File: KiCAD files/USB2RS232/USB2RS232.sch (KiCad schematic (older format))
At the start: 8 parts

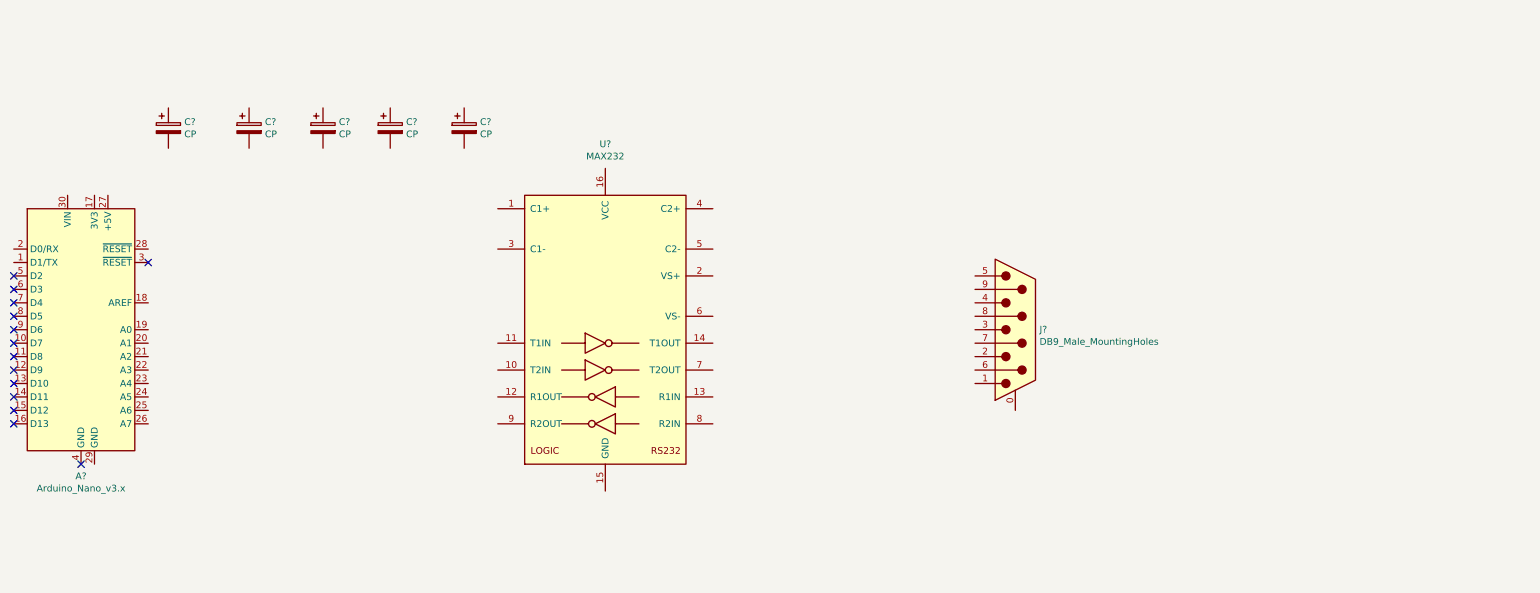
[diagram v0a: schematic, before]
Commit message: Update USB2RS232.sch
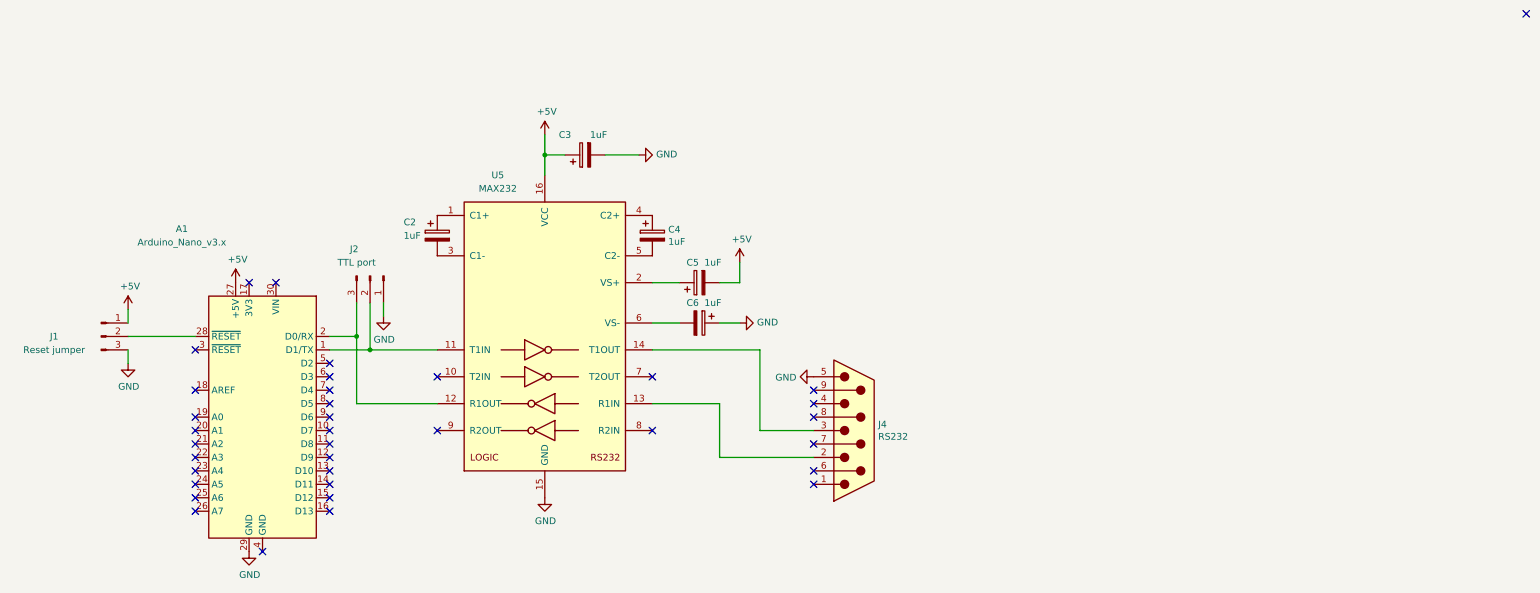
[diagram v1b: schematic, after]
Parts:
- removed A?: Arduino_Nano_v3.x, Module:Arduino_Nano, symbol MCU_Module:Arduino_Nano_v3.x
- removed C? (x5): CP, symbol Device:CP
- removed J?: DB9_Male_MountingHoles, symbol Connector:DB9_Male_MountingHoles
- removed U?: MAX232, symbol Interface_UART:MAX232
- added A1: Arduino_Nano_v3.x, Module:Arduino_Nano, symbol MCU_Module:Arduino_Nano_v3.x
- added C2, C3, C4, C5, C6: 1uF, Capacitor_THT:CP_Radial_D7.5mm_P2.50mm, symbol Device:CP
- added J1: Reset jumper, Connector_PinHeader_2.54mm:PinHeader_1x03_P2.54mm_Horizontal, symbol Connector:Conn_01x03_Male
- added J2: TTL port, Connector_PinHeader_2.54mm:PinHeader_1x03_P2.54mm_Horizontal, symbol Connector:Conn_01x03_Male
- added J4: RS232, Connector_Dsub:DSUB-9_Male_Horizontal_P2.77x2.54mm_EdgePinOffset9.40mm, symbol Connector:DB9_Male
- added U5: MAX232, Package_DIP:DIP-16_W7.62mm_LongPads, symbol Interface_UART:MAX232
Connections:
- new net: C2.1, U5.1 (C1+)
- new net: A1.1 (D1/TX), J2.2 (Pin_2), U5.11 (T1IN)
- new net: A1.2 (D0/RX), J2.3 (Pin_3), U5.12 (R1OUT)
- new net: J4.2, U5.13 (R1IN)
- new net: J4.3, U5.14 (T1OUT)
- new net: C5.1, U5.2 (VS+)
- new net: C2.2, U5.3 (C1-)
- new net: C4.1, U5.4 (C2+)
- new net: C4.2, U5.5 (C2-)
- new net: C6.2, U5.6 (VS-)
- new net: A1.28 (~RESET), J1.2 (Pin_2)
- new net +5V: A1.27 (+5V), C3.1, C5.2, J1.1 (Pin_1), U5.16 (VCC)
- new net GND: A1.29 (GND), C3.2, C6.1, J1.3 (Pin_3), J2.1 (Pin_1), J4.5, U5.15 (GND)
- no-connect marks 14 -> 36

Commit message: Update USB2RS232.sch
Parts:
- C2, C3, C4, C5, C6: footprint Capacitor_THT:CP_Radial_D7.5mm_P2.50mm -> Capacitor_THT:CP_Radial_D5.0mm_P2.50mm
- J1, J2: footprint Connector_PinHeader_2.54mm:PinHeader_1x03_P2.54mm_Horizontal -> Connector_PinSocket_2.54mm:PinSocket_1x03_P2.54mm_Vertical
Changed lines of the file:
@@
 F 0 "C4" H 6868 2796 50  0000 L CNN
 F 1 "1uF" H 6868 2705 50  0000 L CNN
-F 2 "Capacitor_THT:CP_Radial_D7.5mm_P2.50mm" H 6788 2600 50  0001 C CNN
+F 2 "Capacitor_THT:CP_Radial_D5.0mm_P2.50mm" H 6788 2600 50  0001 C CNN
 F 3 "~" H 6750 2750 50  0001 C CNN
 	1    6750 2750
@@
 F 0 "C2" H 4900 2850 50  0000 L CNN
 F 1 "1uF" H 4900 2750 50  0000 L CNN
-F 2 "Capacitor_THT:CP_Radial_D7.5mm_P2.50mm" H 5188 2600 50  0001 C CNN
+F 2 "Capacitor_THT:CP_Radial_D5.0mm_P2.50mm" H 5188 2600 50  0001 C CNN
 F 3 "~" H 5150 2750 50  0001 C CNN
 	1    5150 2750
@@
 F 0 "C5" V 7250 3150 50  0000 C CNN
 F 1 "1uF" V 7250 3000 50  0000 C CNN
-F 2 "Capacitor_THT:CP_Radial_D7.5mm_P2.50mm" H 7138 2950 50  0001 C CNN
+F 2 "Capacitor_THT:CP_Radial_D5.0mm_P2.50mm" H 7138 2950 50  0001 C CNN
 F 3 "~" H 7100 3100 50  0001 C CNN
 	1    7100 3100
@@
 F 0 "C6" V 6950 3350 50  0000 C CNN
 F 1 "1uF" V 6950 3500 50  0000 C CNN
-F 2 "Capacitor_THT:CP_Radial_D7.5mm_P2.50mm" H 7138 3250 50  0001 C CNN
+F 2 "Capacitor_THT:CP_Radial_D5.0mm_P2.50mm" H 7138 3250 50  0001 C CNN
 F 3 "~" H 7100 3400 50  0001 C CNN
 	1    7100 3400
@@
 F 0 "C3" V 6400 2300 50  0000 C CNN
 F 1 "1uF" V 6400 2050 50  0000 C CNN
-F 2 "Capacitor_THT:CP_Radial_D7.5mm_P2.50mm" H 6288 2000 50  0001 C CNN
+F 2 "Capacitor_THT:CP_Radial_D5.0mm_P2.50mm" H 6288 2000 50  0001 C CNN
 F 3 "~" H 6250 2150 50  0001 C CNN
 	1    6250 2150
@@
 F 0 "J1" H 2300 3500 50  0000 C CNN
 F 1 "Reset jumper" H 2300 3400 50  0000 C CNN
-F 2 "Connector_PinHeader_2.54mm:PinHeader_1x03_P2.54mm_Horizontal" H 2650 3500 50  0001 C CNN
+F 2 "Connector_PinSocket_2.54mm:PinSocket_1x03_P2.54mm_Vertical" H 2650 3500 50  0001 C CNN
 F 3 "~" H 2650 3500 50  0001 C CNN
 	1    2650 3500
@@
 F 0 "J2" V 4450 2900 50  0000 L CNN
 F 1 "TTL port" V 4550 2950 50  0000 C CNN
-F 2 "Connector_PinHeader_2.54mm:PinHeader_1x03_P2.54mm_Horizontal" H 4650 3050 50  0001 C CNN
+F 2 "Connector_PinSocket_2.54mm:PinSocket_1x03_P2.54mm_Vertical" H 4650 3050 50  0001 C CNN
 F 3 "~" H 4650 3050 50  0001 C CNN
 	1    4650 3050
